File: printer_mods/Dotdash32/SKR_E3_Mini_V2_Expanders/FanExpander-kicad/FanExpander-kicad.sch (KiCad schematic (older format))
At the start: 65 parts, among them J0 FAN0, J1 FAN1, J10 FAN0_IN, J11 HI_PWR_IN, J2 FAN2, J3 FAN3, J4 FAN4, J5 FAN5, J6 FAN6, J7 FAN7, J8 EXP1_IN, J9 5V_In, Q1 IRLML6344, Q2 IRLML6344, Q3 IRLML6344, Q4 IRLML6344, Q5 IRLML6344, Q6 IRLML6344, Q7 IRLML6344

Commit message: feat: re-routing, pre-terminal blocks
A bunch of routing work, but i'm not fully happy with it, still.
new plan is to mess around and add back the terminal blocks, as well
as move back to full size ATM fuses.
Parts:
- added MH1: MountingHole, Mounting_Holes:MountingHole_3.2mm_M3_Pad, symbol Mechanical:MountingHole_Pad
- JP10: footprint Jumper:SolderJumper-3_P1.3mm_Open_RoundedPad1.0x1.5mm_NumberLabels -> Pin_Headers:Pin_Header_Straight_1x03_Pitch1.00mm
- renumbered MH1 to MH2, MH2 to MH3
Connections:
- wire segments 208 -> 212
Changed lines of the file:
@@
 Wire Wire Line
 	550  1450 850  1450
-Text Label 550  1450 0    50   ~ 0
+Text Label 550  1650 0    50   ~ 0
 FAN1
 Wire Wire Line
@@
 Text Label 550  1550 0    50   ~ 0
 FAN2
-Text Label 550  1650 0    50   ~ 0
+Text Label 550  1750 0    50   ~ 0
 FAN3
-Text Label 550  1750 0    50   ~ 0
+Text Label 550  1450 0    50   ~ 0
 FAN4
-Text Label 1650 1450 2    50   ~ 0
+Text Label 1650 1650 2    50   ~ 0
 FAN5
 $Comp
@@
 P 2150 1650
 F 0 "JP10" V 2196 1718 50  0000 L CNN
-F 1 "FAN_SEL" V 2105 1718 50  0000 L CNN
-F 2 "Jumper:SolderJumper-3_P1.3mm_Open_RoundedPad1.0x1.5mm_NumberLabels" H 2150 1650 50  0001 C CNN
+F 1 "FAN_SEL" V 1850 1550 50  0000 L CNN
+F 2 "Pin_Headers:Pin_Header_Straight_1x03_Pitch1.00mm" H 2150 1650 50  0001 C CNN
 F 3 "~" H 2150 1650 50  0001 C CNN
 	1    2150 1650
@@
 Wire Wire Line
 	1350 1550 1900 1550
-Text Label 1650 1650 2    50   ~ 0
+Text Label 1650 1450 2    50   ~ 0
 FAN6
-Wire Wire Line
-	2300 1650 2550 1650
 Text Label 2550 1650 2    50   ~ 0
 FAN7
@@
 Wire Wire Line
 	2200 7650 2300 7650
-Text Label 1450 5650 0    50   ~ 0
-LED_Drive
-Text Label 750  6900 0    50   ~ 0
+Text Label 1600 7150 0    50   ~ 0
 FAN5
-Text Label 900  6300 0    50   ~ 0
-FAN4
-Text Label 750  6800 0    50   ~ 0
+Text Label 1600 7250 0    50   ~ 0
 FAN7
-Text Label 900  6400 0    50   ~ 0
-FAN6
 $Comp
 L Connector_Generic:Conn_01x02 J10
@@
 	3100 1300 3450 1300
 $Comp
-L Mechanical:MountingHole_Pad MH1
+L Mechanical:MountingHole_Pad MH2
 U 1 1 620EB36C
 P 6050 4650
-F 0 "MH1" V 6004 4800 50  0000 L CNN
+F 0 "MH2" V 6004 4800 50  0000 L CNN
 F 1 "MountingHole" V 6095 4800 50  0000 L CNN
 F 2 "Mounting_Holes:MountingHole_3.2mm_M3_Pad" H 6050 4650 50  0001 C CNN
@@
 $EndComp
 $Comp
-L Mechanical:MountingHole_Pad MH2
+L Mechanical:MountingHole_Pad MH3
 U 1 1 620ED7F0
 P 6050 4850
-F 0 "MH2" V 6004 5000 50  0000 L CNN
+F 0 "MH3" V 6004 5000 50  0000 L CNN
 F 1 "MountingHole" V 6095 5000 50  0000 L CNN
 F 2 "Mounting_Holes:MountingHole_3.2mm_M3_Pad" H 6050 4850 50  0001 C CNN
@@
 $EndComp
 Wire Wire Line
-	2550 4650 2550 4750
-Wire Wire Line
-	2550 4750 2450 4750
-Wire Wire Line
-	2450 4850 2800 4850
-Wire Wire Line
-	2800 4650 2800 4850
+	2800 4650 2800 4750
 Wire Wire Line
 	1850 4950 1850 4850
@@
 $EndComp
 Wire Wire Line
-	2100 5600 2100 6350
-Wire Wire Line
 	2300 7350 2200 7350
 Wire Wire Line
@@
 Wire Wire Line
 	2200 7350 2100 7350
-Wire Wire Line
-	2000 5950 2000 7750
-Wire Wire Line
-	2300 6650 1450 6650
-Wire Wire Line
-	2300 5650 1450 5650
-Wire Wire Line
-	1450 5650 1450 6650
-Wire Wire Line
-	2300 6450 2200 6450
-Wire Wire Line
-	2300 6550 2200 6550
-Wire Wire Line
-	2200 6550 2200 6450
-Wire Wire Line
-	2300 6350 2200 6350
-Wire Wire Line
-	2300 6250 2200 6250
-Wire Wire Line
-	2200 6250 2200 6350
-Connection ~ 2200 6350
-Wire Wire Line
-	2200 6350 2100 6350
+$Comp
+L Mechanical:MountingHole_Pad MH1
+U 1 1 626DA97D
+P 5650 4850
+F 0 "MH1" V 5604 5000 50  0000 L CNN
+F 1 "MountingHole" V 5695 5000 50  0000 L CNN
+F 2 "Mounting_Holes:MountingHole_3.2mm_M3_Pad" H 5650 4850 50  0001 C CNN
+F 3 "~" H 5650 4850 50  0001 C CNN
+	1    5650 4850
+	0    -1   -1   0
+$EndComp
+Wire Wire Line
+	5750 4850 5850 4850
+Wire Wire Line
+	2300 5650 1600 5650
+Text Label 1600 5650 0    50   ~ 0
+FAN4
+Wire Wire Line
+	2100 5600 2100 6350
+Wire Wire Line
+	2300 6350 2100 6350
 Connection ~ 2100 6350
 Wire Wire Line
-	1900 5600 1900 6450
-Wire Wire Line
-	2100 6350 2100 7350
-Wire Wire Line
-	2200 6450 1900 6450
-Connection ~ 2200 6450
-Connection ~ 1900 6450
-Wire Wire Line
-	1900 6450 1900 7650
+	2100 6350 2100 6450
+Wire Wire Line
+	2300 6850 1450 6850
+Wire Wire Line
+	2550 4650 2550 4850
+Wire Wire Line
+	2450 4850 2550 4850
+Wire Wire Line
+	2450 4750 2800 4750
+Wire Wire Line
+	2300 6550 1900 6550
+Connection ~ 1900 6550
+Wire Wire Line
+	1900 6550 1900 6650
+Wire Wire Line
+	2300 6650 1900 6650
+Connection ~ 1900 6650
+Wire Wire Line
+	1900 6650 1900 7650
+Wire Wire Line
+	1900 5600 1900 6550
+Wire Wire Line
+	2300 6450 2100 6450
+Connection ~ 2100 6450
+Wire Wire Line
+	2100 6450 2100 7350
+Wire Wire Line
+	2300 7150 1600 7150
+Wire Wire Line
+	2300 7250 1600 7250
+Text Label 1600 5850 0    50   ~ 0
+FAN6
+Wire Wire Line
+	2300 5850 1600 5850
+Text Label 1450 5950 0    50   ~ 0
+LED_Drive
+Wire Wire Line
+	1450 5950 1450 6850
+Wire Wire Line
+	2300 5750 1600 5750
+Text Label 1600 5750 0    50   ~ 0
+FAN2
+Wire Wire Line
+	1450 5950 2300 5950
+Wire Wire Line
+	2000 7750 2000 5550
+Wire Wire Line
+	2550 1650 2300 1650
 $EndSCHEMATC

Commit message: test: move to ATM fuses, keep breakaway
I don't think the breakaway is actuall worthwhile??
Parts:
- removed J11: HI_PWR_IN, Pin_Headers:Pin_Header_Straight_2x02_Pitch2.54mm, symbol Connector_Generic:Conn_02x02_Odd_Even
- added J12: HI_PWR_IN, Connectors_Terminal_Blocks:TerminalBlock_bornier-3_P5.08mm, symbol Connector_Generic:Conn_01x03
- added JP12: FAN0_CTRL, Jumper:SolderJumper-2_P1.3mm_Bridged2Bar_RoundedPad1.0x1.5mm, symbol Jumper:SolderJumper_2_Open
- added SPL2: Conn_01x37, Pin_Headers:Pin_Header_Straight_1x37_Pitch1.00mm, symbol Connector_Generic:Conn_01x37
- added SPL3: Conn_01x36, Pin_Headers:Pin_Header_Straight_1x36_Pitch1.00mm, symbol Connector_Generic:Conn_01x36
- F1, F2: footprint Fuse:Fuse_2920_7451Metric -> Fuse:Fuseholder_Blade_Mini_Keystone_3544
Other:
- note removed: "far from connector"
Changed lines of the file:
@@
 F 0 "F2" V 2150 4100 50  0000 L CNN
 F 1 "Polyfuse-2.5A" V 2250 3950 50  0000 L CNN
-F 2 "Fuse:Fuse_2920_7451Metric" H 2400 3950 50  0001 L CNN
+F 2 "Fuse:Fuseholder_Blade_Mini_Keystone_3544" H 2400 3950 50  0001 L CNN
 F 3 "~" H 2350 4150 50  0001 C CNN
 	1    2350 4150
@@
 $EndComp
 Wire Wire Line
-	4350 1500 4200 1500
-Wire Wire Line
-	4200 1500 4200 1600
-Wire Wire Line
-	3500 1600 3450 1600
-Wire Wire Line
-	3800 1600 4200 1600
-Text Label 3850 1600 0    50   ~ 0
+	4350 1500 4250 1500
+Text Label 3900 1600 0    50   ~ 0
 FAN0_Dr
 Text Notes 3050 1100 0    100  ~ 0
@@
 Text Label 3100 1300 0    50   ~ 0
 LED_Drive
-Wire Wire Line
-	3100 1300 3450 1300
 $Comp
 L Mechanical:MountingHole_Pad MH2
@@
 	5850 4650 5850 4850
 Connection ~ 5850 4850
-$Comp
-L Connector_Generic:Conn_02x02_Odd_Even J11
-U 1 1 61E53681
-P 2150 4750
-F 0 "J11" H 2200 4967 50  0000 C CNN
-F 1 "HI_PWR_IN" H 2200 4876 50  0000 C CNN
-F 2 "Pin_Headers:Pin_Header_Straight_2x02_Pitch2.54mm" H 2150 4750 50  0001 C CNN
-F 3 "~" H 2150 4750 50  0001 C CNN
-	1    2150 4750
-	1    0    0    -1
-$EndComp
-$Comp
-L power:GND #PWR0112
-U 1 1 61E55553
-P 1850 4950
-F 0 "#PWR0112" H 1850 4700 50  0001 C CNN
-F 1 "GND" H 1855 4777 50  0000 C CNN
-F 2 "" H 1850 4950 50  0001 C CNN
-F 3 "" H 1850 4950 50  0001 C CNN
-	1    1850 4950
-	1    0    0    -1
-$EndComp
-$Comp
-L power:+5V #PWR0113
-U 1 1 61E57DBE
-P 2550 4650
-F 0 "#PWR0113" H 2550 4500 50  0001 C CNN
-F 1 "+5V" H 2565 4823 50  0000 C CNN
-F 2 "" H 2550 4650 50  0001 C CNN
-F 3 "" H 2550 4650 50  0001 C CNN
-	1    2550 4650
-	1    0    0    -1
-$EndComp
-$Comp
-L power:+24V #PWR0114
-U 1 1 61E57DC4
-P 2800 4650
-F 0 "#PWR0114" H 2800 4500 50  0001 C CNN
-F 1 "+24V" H 2815 4823 50  0000 C CNN
-F 2 "" H 2800 4650 50  0001 C CNN
-F 3 "" H 2800 4650 50  0001 C CNN
-	1    2800 4650
-	1    0    0    -1
-$EndComp
-Wire Wire Line
-	2800 4650 2800 4750
-Wire Wire Line
-	1850 4950 1850 4850
-Wire Wire Line
-	1850 4750 1950 4750
-Wire Wire Line
-	1850 4850 1950 4850
-Connection ~ 1850 4850
-Wire Wire Line
-	1850 4850 1850 4750
 Wire Notes Line
 	4900 900  4900 5250
@@
 Text Notes 4950 4500 0    100  ~ 0
 Mounting Holes
-Text Notes 4950 4600 0    50   ~ 0
-far from connector
 Text Notes 600  5600 0    100  ~ 0
 Breakaway\nConnector
@@
 Text Notes 1850 2600 0    50   ~ 0
 SKR 2 EXP2\nPA6  | PA5\nPE7  | PA4\nPB2  | PA7\nPC4  | RST\nGND  | NC
-Text Notes 3050 2350 0    50   ~ 0
+Text Notes 2550 -150 0    50   ~ 0
 Fan0 is a Passthrough Fan.\nNo control is exerted on this fan.\nIt can either select the voltage \nfor a fan on the primary board,\nor can hve a voltage selectable \nalways on fan.
-Text Notes 500  5000 0    50   ~ 0
+Text Notes -1150 5250 0    50   ~ 0
 These pins bypass the PTC Fuses,\nallowing higher current devices\nto be run.  An external fuse \nshould be used, and Fans 7-6\nprefered (shorter traces)
 Wire Notes Line width 12 style solid
@@
 F 0 "F1" V 2150 3050 50  0000 L CNN
 F 1 "Polyfuse-2.5A" V 2250 2900 50  0000 L CNN
-F 2 "Fuse:Fuse_2920_7451Metric" H 2400 2900 50  0001 L CNN
+F 2 "Fuse:Fuseholder_Blade_Mini_Keystone_3544" H 2400 2900 50  0001 L CNN
 F 3 "~" H 2350 3100 50  0001 C CNN
 	1    2350 3100
@@
 	2300 6850 1450 6850
 Wire Wire Line
-	2550 4650 2550 4850
-Wire Wire Line
-	2450 4850 2550 4850
-Wire Wire Line
-	2450 4750 2800 4750
-Wire Wire Line
 	2300 6550 1900 6550
 Connection ~ 1900 6550
@@
 Wire Wire Line
 	2550 1650 2300 1650
+$Comp
+L Jumper:SolderJumper_2_Open JP12
+U 1 1 61D688A0
+P 4500 1850
+F 0 "JP12" H 4500 2055 50  0000 C CNN
+F 1 "FAN0_CTRL" H 4500 1964 50  0000 C CNN
+F 2 "Jumper:SolderJumper-2_P1.3mm_Bridged2Bar_RoundedPad1.0x1.5mm" H 4500 1850 50  0001 C CNN
+F 3 "~" H 4500 1850 50  0001 C CNN
+	1    4500 1850
+	1    0    0    -1
+$EndComp
+$Comp
+L power:GND #PWR025
+U 1 1 61DE8DF2
+P 4700 1900
+F 0 "#PWR025" H 4700 1650 50  0001 C CNN
+F 1 "GND" H 4705 1727 50  0000 C CNN
+F 2 "" H 4700 1900 50  0001 C CNN
+F 3 "" H 4700 1900 50  0001 C CNN
+	1    4700 1900
+	1    0    0    -1
+$EndComp
+Wire Wire Line
+	3800 1600 4250 1600
+Wire Wire Line
+	4250 1500 4250 1600
+Wire Wire Line
+	4650 1850 4700 1850
+Wire Wire Line
+	4700 1850 4700 1900
+Wire Wire Line
+	3450 1300 3100 1300
+$Comp
+L power:GND #PWR0107
+U 1 1 61EDFEE1
+P 2000 4950
+F 0 "#PWR0107" H 2000 4700 50  0001 C CNN
+F 1 "GND" H 2005 4777 50  0000 C CNN
+F 2 "" H 2000 4950 50  0001 C CNN
+F 3 "" H 2000 4950 50  0001 C CNN
+	1    2000 4950
+	1    0    0    -1
+$EndComp
+Wire Wire Line
+	1950 4800 2000 4800
+Wire Wire Line
+	1950 4900 2550 4900
+Wire Wire Line
+	1950 4700 2550 4700
+Text Label 2550 4700 2    50   ~ 0
+5V_unFused
+Text Label 2550 4900 2    50   ~ 0
+24V_unFused
+$Comp
+L Connector_Generic:Conn_01x03 J12
+U 1 1 61FDDC98
+P 1750 4800
+F 0 "J12" H 1668 4475 50  0000 C CNN
+F 1 "HI_PWR_IN" H 1668 4566 50  0000 C CNN
+F 2 "Connectors_Terminal_Blocks:TerminalBlock_bornier-3_P5.08mm" H 1750 4800 50  0001 C CNN
+F 3 "~" H 1750 4800 50  0001 C CNN
+	1    1750 4800
+	-1   0    0    1
+$EndComp
+Wire Wire Line
+	2000 4950 2000 4800
+$Comp
+L Connector_Generic:Conn_01x36 SPL3
+U 1 1 61D71BE5
+P 6100 6100
+F 0 "SPL3" V 6317 6046 50  0000 C CNN
+F 1 "Conn_01x36" V 6226 6046 50  0000 C CNN
+F 2 "Pin_Headers:Pin_Header_Straight_1x36_Pitch1.00mm" H 6100 6100 50  0001 C CNN
+F 3 "~" H 6100 6100 50  0001 C CNN
+	1    6100 6100
+	0    -1   -1   0
+$EndComp
+$Comp
+L Connector_Generic:Conn_01x37 SPL2
+U 1 1 61D60D1C
+P 6200 5650
+F 0 "SPL2" V 6417 5646 50  0000 C CNN
+F 1 "Conn_01x37" V 6326 5646 50  0000 C CNN
+F 2 "Pin_Headers:Pin_Header_Straight_1x37_Pitch1.00mm" H 6200 5650 50  0001 C CNN
+F 3 "~" H 6200 5650 50  0001 C CNN
+	1    6200 5650
+	0    -1   -1   0
+$EndComp
+Wire Wire Line
+	3450 1600 3500 1600
+Wire Wire Line
+	4250 1600 4250 1850
+Wire Wire Line
+	4250 1850 4350 1850
+Connection ~ 4250 1600
 $EndSCHEMATC

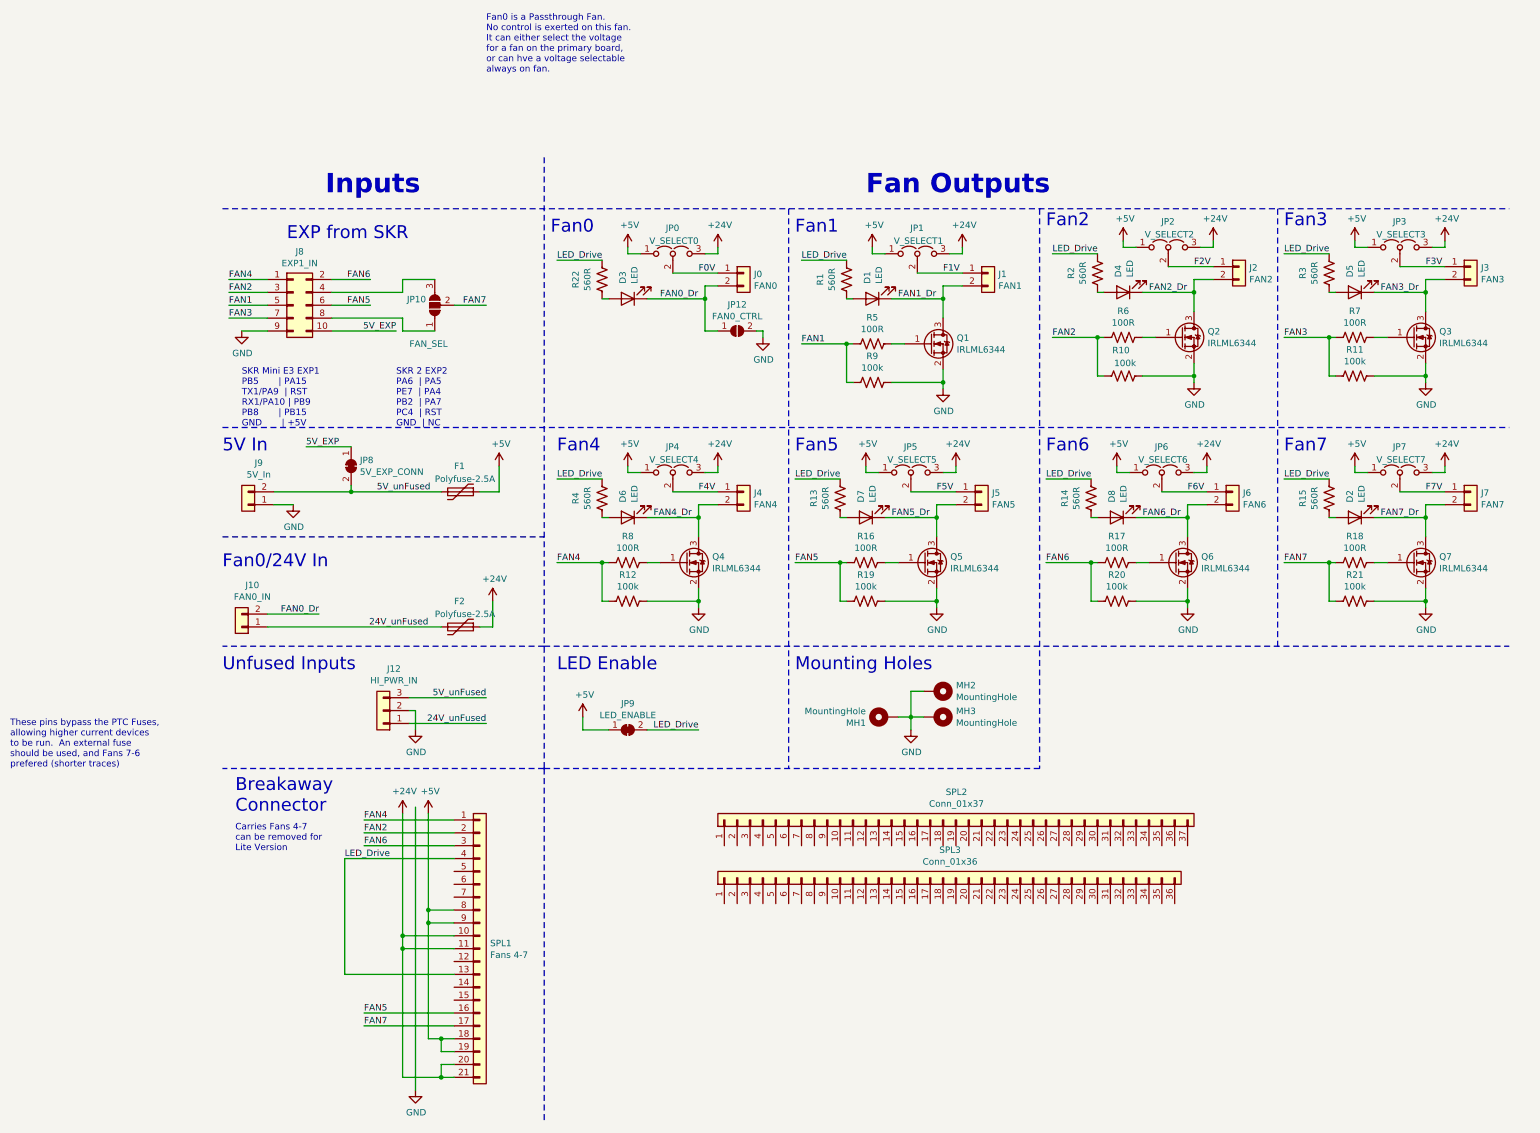
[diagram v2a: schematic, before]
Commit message: feat: new layout with screw terminals and jumpers
add more jumpers to make any kind of voltage selection more easy,
particularly for fan0, either always on or cutting 24V in

no routing done yet lol
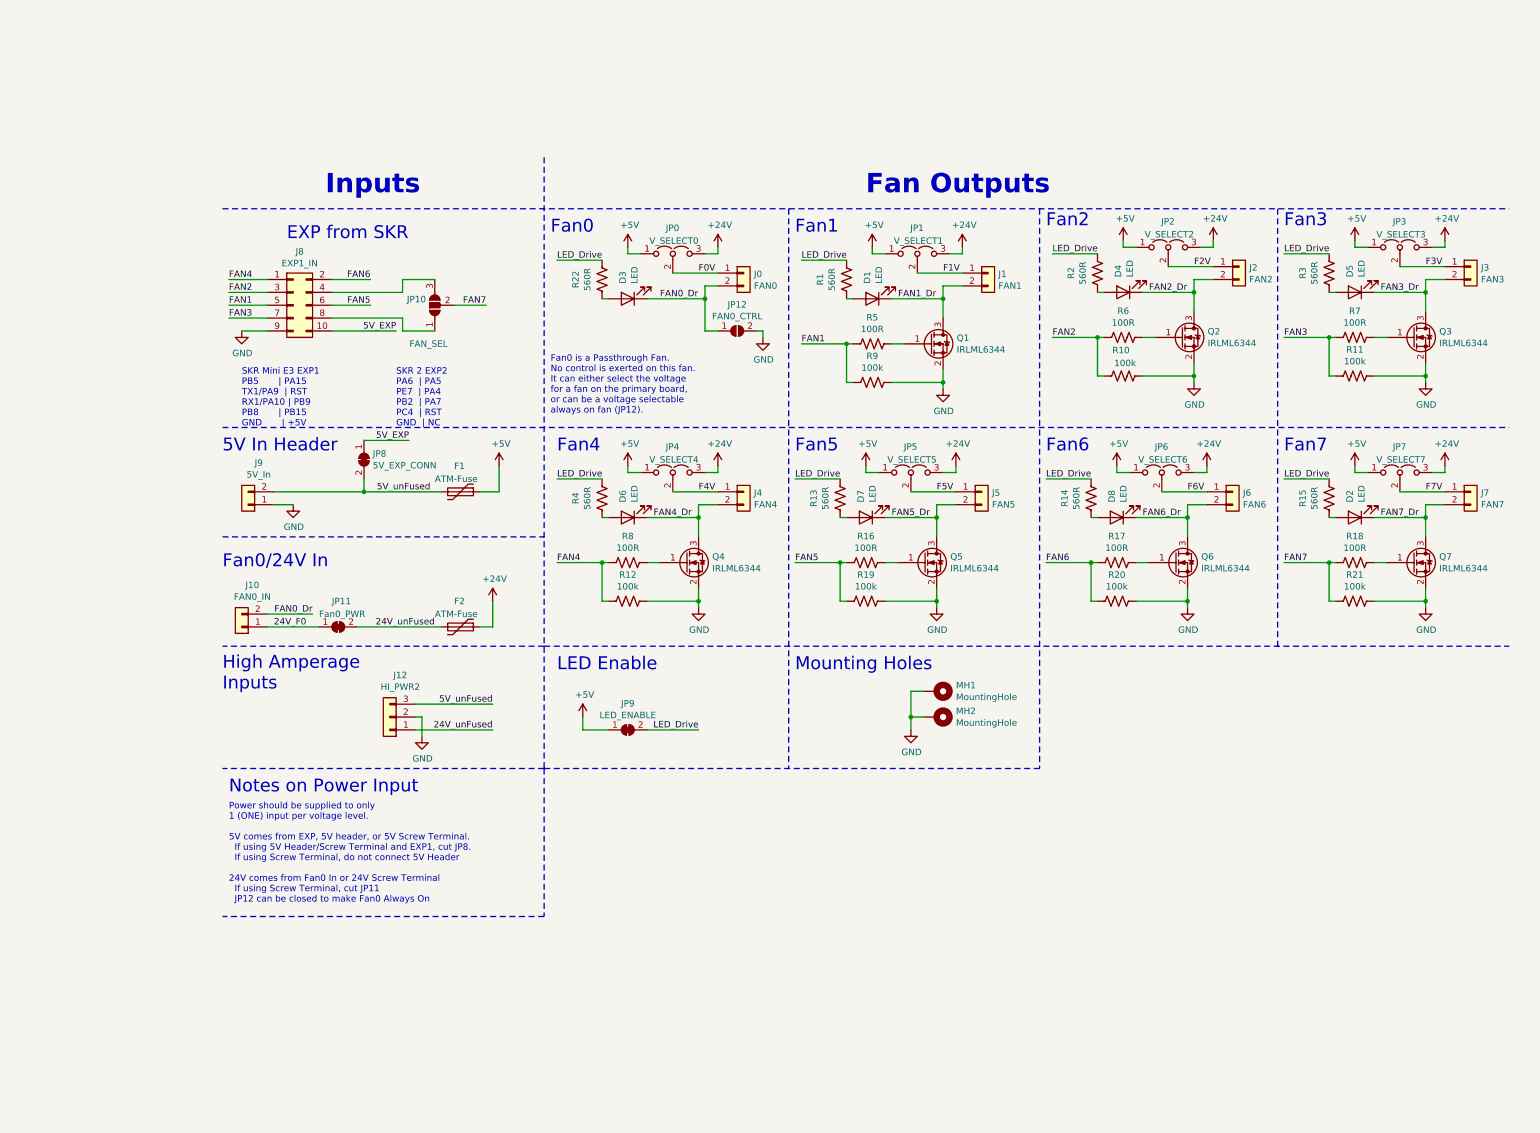
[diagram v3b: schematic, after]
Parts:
- removed MH3: MountingHole, Mounting_Holes:MountingHole_3.2mm_M3_Pad, symbol Mechanical:MountingHole_Pad
- removed SPL1: Fans 4-7, Pin_Headers:Pin_Header_Straight_1x21_Pitch1.00mm, symbol Connector_Generic:Conn_01x21
- removed SPL2: Conn_01x37, Pin_Headers:Pin_Header_Straight_1x37_Pitch1.00mm, symbol Connector_Generic:Conn_01x37
- removed SPL3: Conn_01x36, Pin_Headers:Pin_Header_Straight_1x36_Pitch1.00mm, symbol Connector_Generic:Conn_01x36
- added JP11: Fan0_PWR, Jumper:SolderJumper-2_P1.3mm_Bridged_RoundedPad1.0x1.5mm, symbol Jumper:SolderJumper_2_Bridged
- F1, F2: value Polyfuse-2.5A -> ATM-Fuse
- J12: value HI_PWR_IN -> HI_PWR2; footprint Connectors_Terminal_Blocks:TerminalBlock_bornier-3_P5.08mm -> TerminalBlock_Pheonix:TerminalBlock_Phoenix_MKDS-1,5-3-5.08_1x03_P5.08mm_Horizontal
- JP10: footprint Pin_Headers:Pin_Header_Straight_1x03_Pitch1.00mm -> Pin_Headers:Pin_Header_Straight_1x03_Pitch1.27mm
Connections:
- net 24V_unFused: now also JP11.2 (B); no longer J10.1 (Pin_1)
- new net 24V_F0: J10.1 (Pin_1), JP11.1 (A)
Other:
- note added: "5V In Header"
- note added: "Fan0 is a Passthrough Fan.\nNo control is exerted on this fan.\nIt can either select the voltage \nfor a fan on the primary board,\nor can be a voltage selectable \nalways on fan (JP12)."
- note added: "High Amperage\nInputs"
- note added: "Notes on Power Input"
- note added: "Power should be supplied to only \n1 (ONE) input per voltage level.\n\n5V comes from EXP, 5V header, or 5V Screw Terminal.\n If using 5V Header/Screw Terminal and EXP1, cut JP8.\n If using Screw Terminal, do not connect 5V Header\n\n24V comes from Fan0 In or 24V Screw Terminal\n If using Screw Terminal, cut JP11\n JP12 can be closed to make Fan0 Always On"
- note removed: "5V In"
- note removed: "Breakaway\nConnector"
- note removed: "Carries Fans 4-7\ncan be removed for \nLite Version"
- note removed: "Fan0 is a Passthrough Fan.\nNo control is exerted on this fan.\nIt can either select the voltage \nfor a fan on the primary board,\nor can hve a voltage selectable \nalways on fan."
- note removed: "These pins bypass the PTC Fuses,\nallowing higher current devices\nto be run. An external fuse \nshould be used, and Fans 7-6\nprefered (shorter traces)"
- note removed: "Unfused Inputs"
- moved on the sheet: JP8, MH1, MH2
